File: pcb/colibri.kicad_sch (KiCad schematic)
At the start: 88 parts

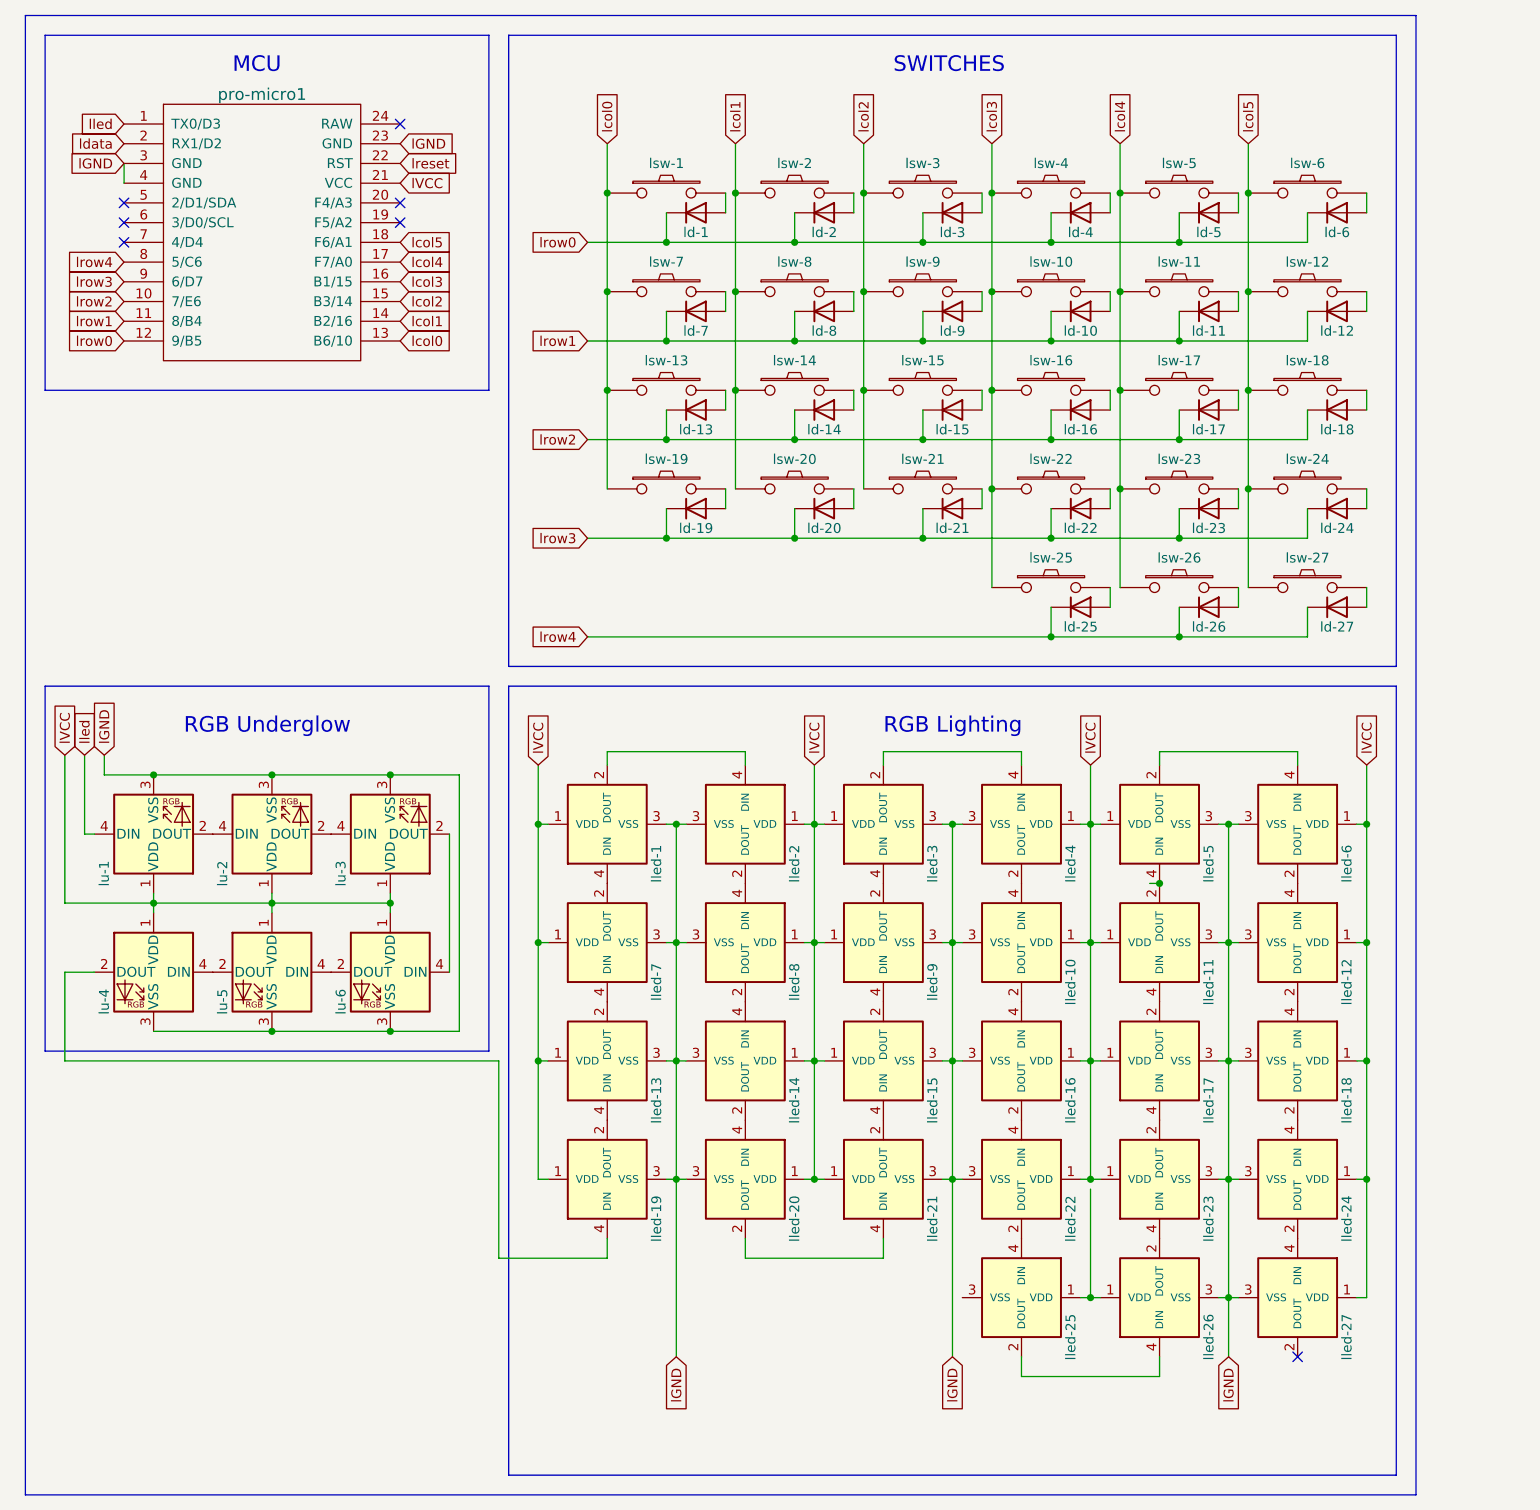
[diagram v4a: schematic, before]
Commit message: better keyboard layout
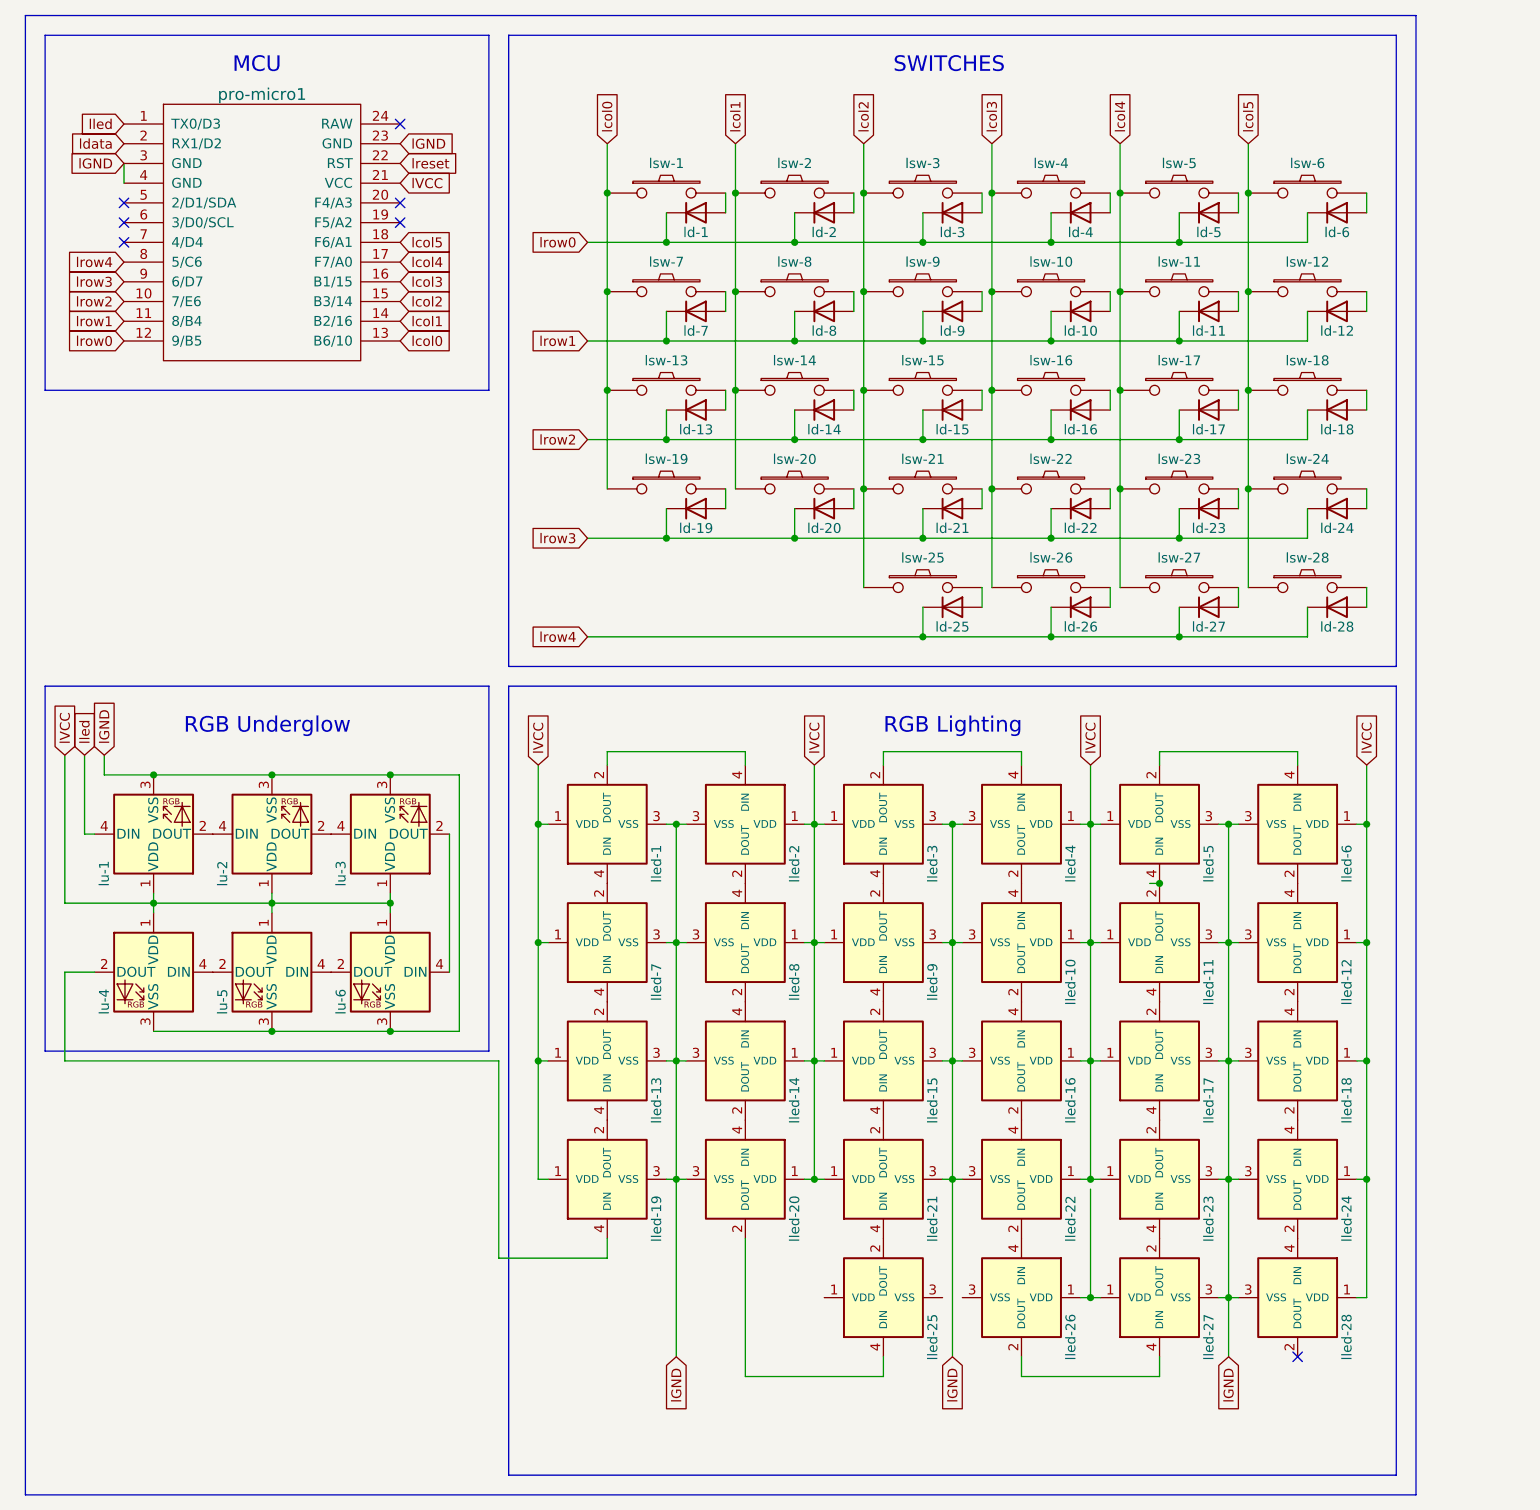
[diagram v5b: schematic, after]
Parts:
- added ld-28: 1N4148W, kbd:D3_SMD_v2, symbol Diode:1N4148W
- added lled-25: YS-SK6812MINI-E, kbd:YS-SK6812MINI-E, symbol kbd:YS-SK6812MINI-E
- added lsw-28: SW_PUSH, kbd:CherryMX_Hotswap_2u, symbol kbd:SW_PUSH
- lsw-1: footprint kbd:CherryMX_Hotswap_1.25U -> kbd:CherryMX_Hotswap
- lsw-13: footprint kbd:CherryMX_Hotswap_1.25U -> kbd:CherryMX_Hotswap_1.75u
- lsw-19: footprint kbd:CherryMX_Hotswap_1.25U -> kbd:CherryMX_Hotswap_2.25u
- lsw-25, lsw-26: footprint kbd:CherryMX_Hotswap -> kbd:CherryMX_Hotswap_1.25u
- lsw-27: footprint kbd:CherryMX_Hotswap_1.5u -> kbd:CherryMX_Hotswap_1.25u
- lsw-7: footprint kbd:CherryMX_Hotswap_1.25U -> kbd:CherryMX_Hotswap_1.5u
- renumbered lled-25 to lled-26, lled-26 to lled-27, lled-27 to lled-28
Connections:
- net lcol2: now also lsw-25.1
- net lcol3: now also lsw-26.1; no longer lsw-25.1
- net lcol4: now also lsw-27.1; no longer lsw-26.1
- net lcol5: now also lsw-28.1; no longer lsw-27.1
- net lrow4: now also ld-28.1 (K)
- net at lled-21.4 (DIN): now also lled-25.2 (DOUT); no longer lled-20.2 (DOUT)
- new net: lled-20.2 (DOUT), lled-25.4 (DIN)
- new net: ld-28.2 (A), lsw-28.2
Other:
- moved on the sheet: ld-25, ld-26, ld-27, lsw-25, lsw-26, lsw-27

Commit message: rows connected
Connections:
- net lcol1: now also lsw-25.1
- net lcol2: now also lsw-26.1; no longer lsw-25.1
- net lcol3: now also lsw-27.1; no longer lsw-26.1
- net lcol4: no longer lsw-27.1
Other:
- moved on the sheet: ld-25, ld-26, ld-27, lsw-25, lsw-26, lsw-27

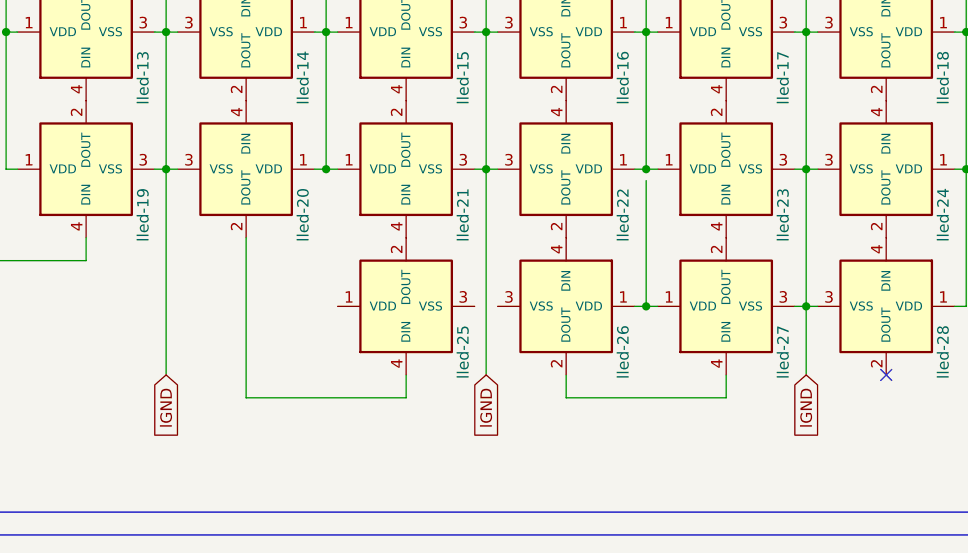
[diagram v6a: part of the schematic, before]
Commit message: all leds connected
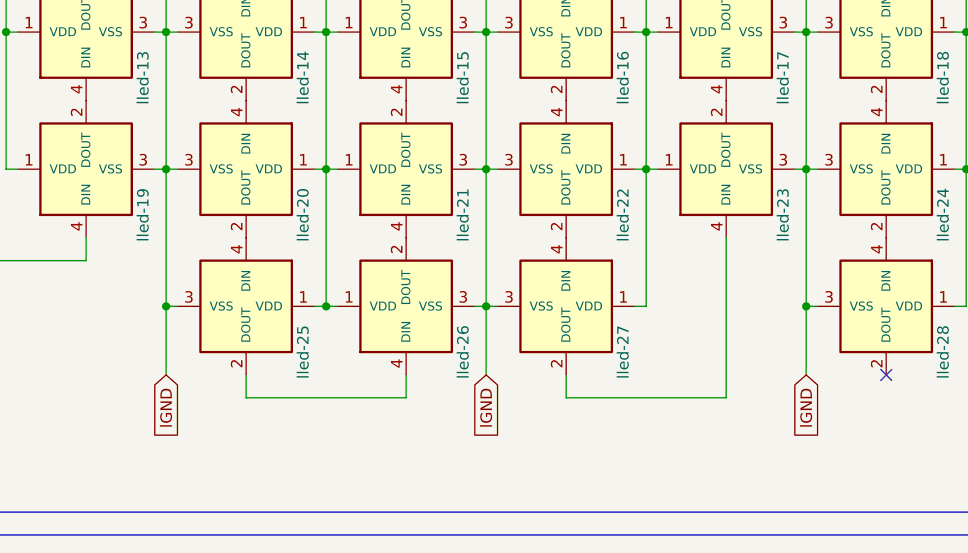
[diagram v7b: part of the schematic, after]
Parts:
- removed lled-27: YS-SK6812MINI-E, kbd:YS-SK6812MINI-E, symbol kbd:YS-SK6812MINI-E
- added lled-25: YS-SK6812MINI-E, kbd:YS-SK6812MINI-E, symbol kbd:YS-SK6812MINI-E
- renumbered lled-25 to lled-26, lled-26 to lled-27
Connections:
- net lGND: now also lled-26.3 (VSS), lled-27.3 (VSS), lled-25.3 (VSS)
- net lVCC: now also lled-26.1 (VDD), lled-27.1 (VDD), lled-25.1 (VDD)
- net at lled-23.4 (DIN): now also lled-27.2 (DOUT)
- net at lled-26.4 (DIN): now also lled-25.2 (DOUT); no longer lled-20.2 (DOUT)
- new net: lled-20.2 (DOUT), lled-25.4 (DIN)
